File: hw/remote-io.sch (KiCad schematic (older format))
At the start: 13 parts, among them P1 CONN_01X02, P10 CONN_01X02, P2 CONN_01X08, P3 CONN_01X08, P5 CONN_02X20

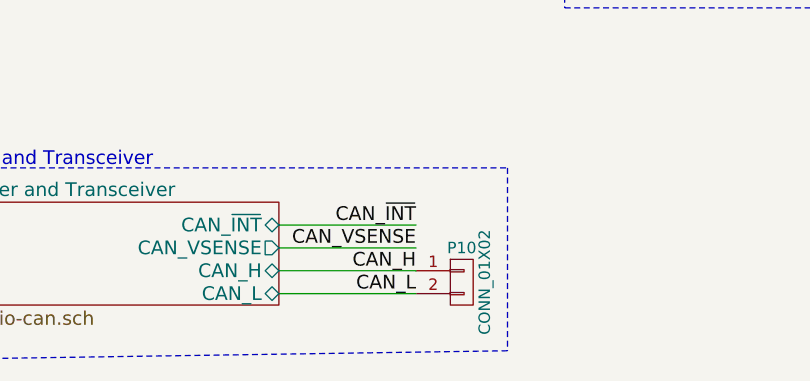
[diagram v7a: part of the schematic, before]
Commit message: Edited board dims to get rid of flex cutout. May need to move conns to other side
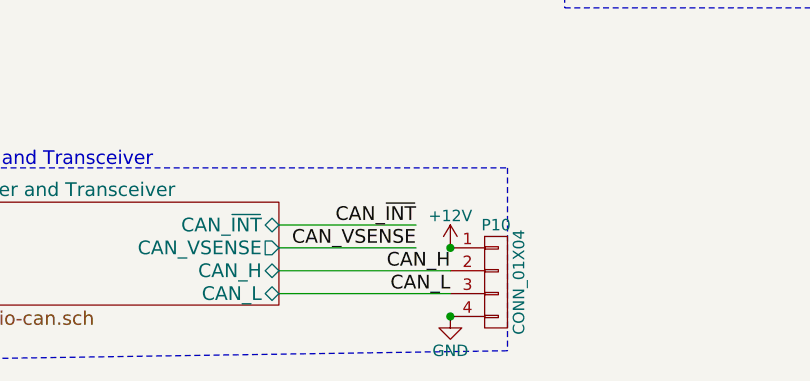
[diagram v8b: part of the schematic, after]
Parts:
- removed P10: CONN_01X02, remote-io:OSTTE020104, symbol CONN_01X02
- added P10: CONN_01X04, remote-io:OSTTE040104, symbol CONN_01X04
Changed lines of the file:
@@
 Text Label 7400 5700 2    60   ~ 0
 CAN_~INT
-Text Label 7400 5900 2    60   ~ 0
+Text Label 7550 5900 2    60   ~ 0
 CAN_H
-Text Label 7400 6000 2    60   ~ 0
+Text Label 7550 6000 2    60   ~ 0
 CAN_L
-$Comp
-L CONN_01X02 P10
-U 1 1 5583C21E
-P 7600 5950
-F 0 "P10" H 7600 6100 50  0000 C CNN
-F 1 "CONN_01X02" V 7700 5950 50  0000 C CNN
-F 2 "remote-io:OSTTE020104" H 7600 5950 60  0001 C CNN
-F 3 "" H 7600 5950 60  0000 C CNN
-	1    7600 5950
-	1    0    0    -1
-$EndComp
 Text Label 8150 2900 0    60   ~ 0
 CAN_~INT
@@
 	6800 5700 7400 5700
 Wire Wire Line
-	6800 5900 7400 5900
-Wire Wire Line
-	6800 6000 7400 6000
+	6800 5900 7550 5900
+Wire Wire Line
+	6800 6000 7550 6000
 Wire Notes Line
 	4450 5450 7800 5450
@@
 Connection ~ 9250 2700
 NoConn ~ 9250 3100
+$Comp
+L CONN_01X04 P10
+U 1 1 5588C101
+P 7750 5950
+F 0 "P10" H 7750 6200 50  0000 C CNN
+F 1 "CONN_01X04" V 7850 5950 50  0000 C CNN
+F 2 "remote-io:OSTTE040104" H 7750 5950 60  0001 C CNN
+F 3 "" H 7750 5950 60  0000 C CNN
+	1    7750 5950
+	1    0    0    -1
+$EndComp
+$Comp
+L +12V #PWR027
+U 1 1 5588C988
+P 7550 5800
+F 0 "#PWR027" H 7550 5650 50  0001 C CNN
+F 1 "+12V" H 7550 5940 50  0000 C CNN
+F 2 "" H 7550 5800 60  0000 C CNN
+F 3 "" H 7550 5800 60  0000 C CNN
+	1    7550 5800
+	1    0    0    -1
+$EndComp
+$Comp
+L GND #PWR028
+U 1 1 5588CAFD
+P 7550 6100
+F 0 "#PWR028" H 7550 5850 50  0001 C CNN
+F 1 "GND" H 7550 5950 50  0000 C CNN
+F 2 "" H 7550 6100 60  0000 C CNN
+F 3 "" H 7550 6100 60  0000 C CNN
+	1    7550 6100
+	1    0    0    -1
+$EndComp
+Connection ~ 7550 5800
+Connection ~ 7550 6100
 $EndSCHEMATC
